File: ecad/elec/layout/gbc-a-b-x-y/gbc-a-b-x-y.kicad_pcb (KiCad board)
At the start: 2 copper layers, 10 parts

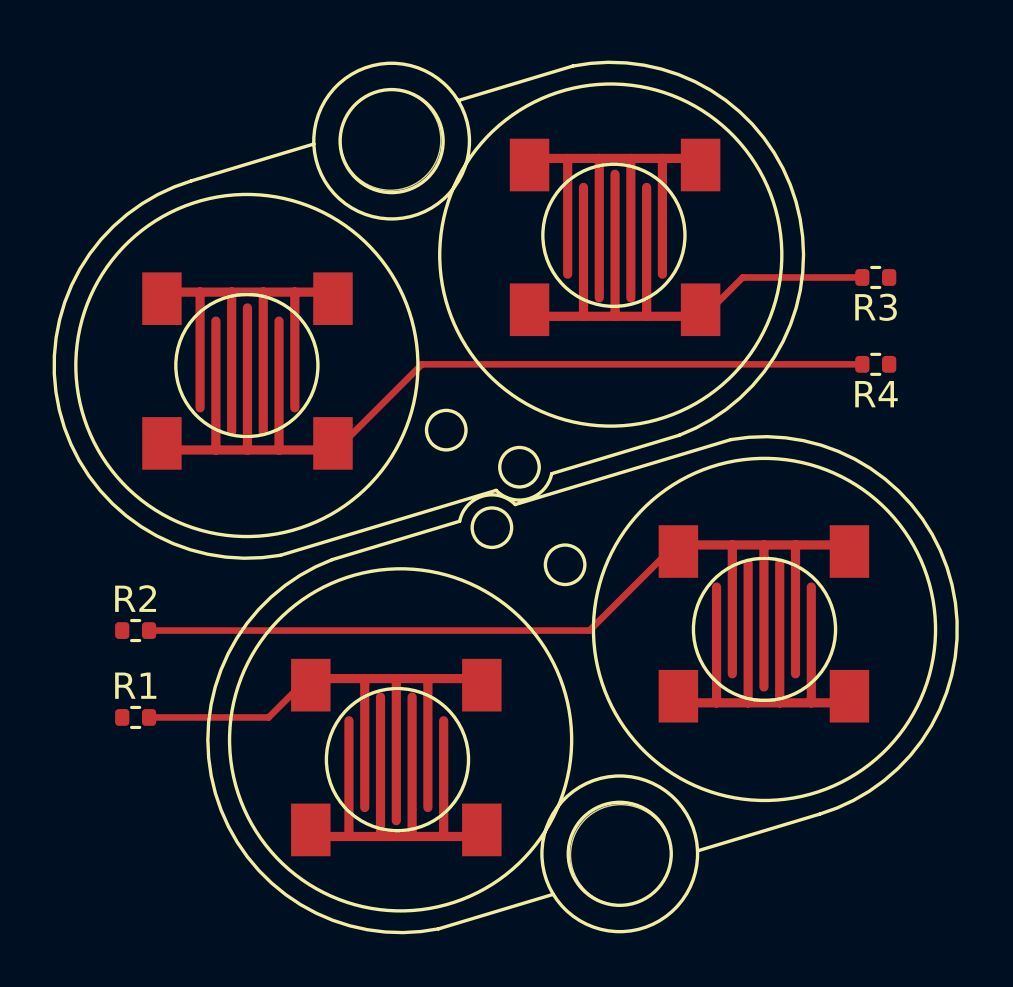
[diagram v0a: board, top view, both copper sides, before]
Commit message: update layouts to use latest footprints and fixed volume buttons and include address pins
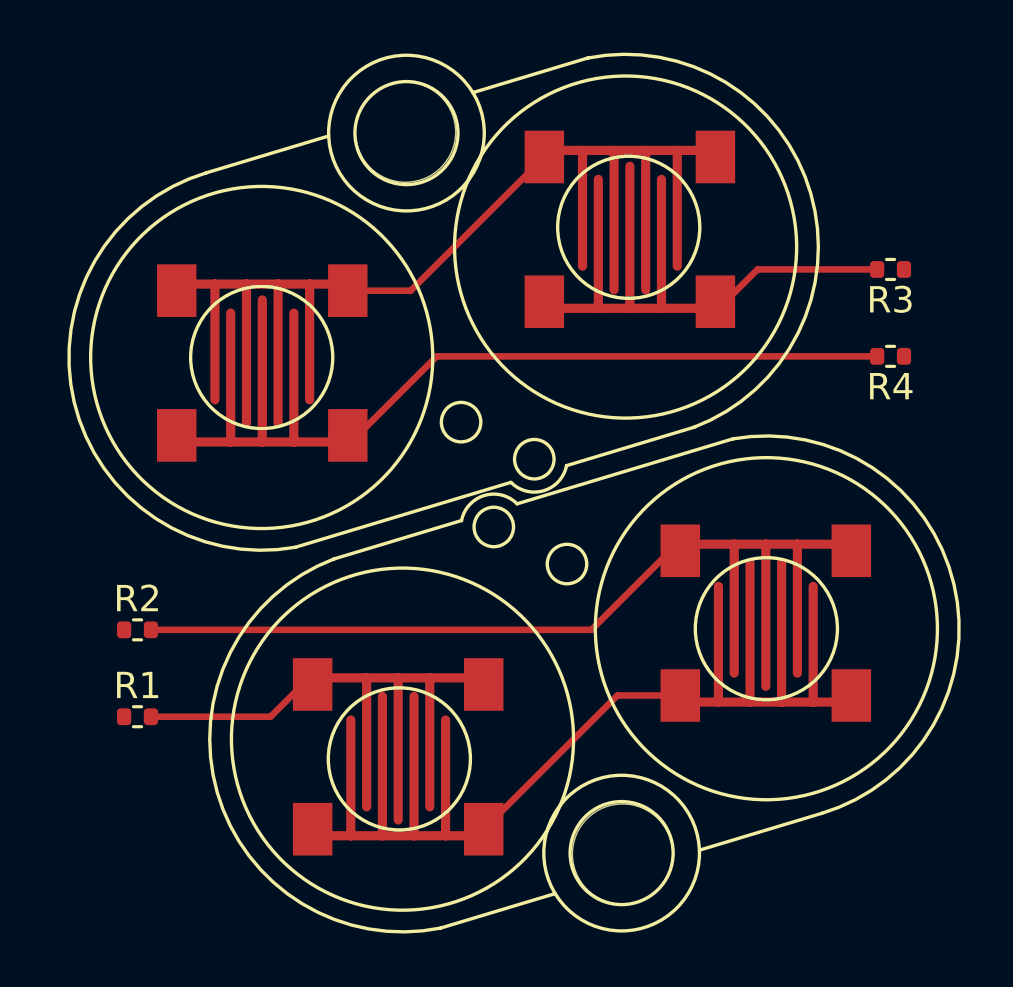
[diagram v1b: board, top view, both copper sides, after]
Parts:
- moved U4 0.64 mm to (179.2, 60.5)
- moved R3 0.64 mm to (196.1, 59.6)
- moved R4 0.64 mm to (196.1, 62.9)
- moved U5 0.64 mm to (186.2, 58.1)
- moved U6 0.64 mm to (172.3, 63.2)
- moved U2 0.08 mm to (177.4, 78.2)
- moved U3 0.08 mm to (191.4, 73.1)
- moved R1 0.08 mm to (167.5, 76.6)
- moved U1 0.08 mm to (184.4, 75.8)
- moved R2 0.08 mm to (167.5, 73.3)
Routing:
- net vcc: track 0.00 -> 19.1 mm

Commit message: Fix/atopile ecad (#82)
* fix(ecad): Fix bugs in atopile version of the design
* Add missing pullup resistors to AW9523 RSTN and INTN lines
* Fix I/O configuration for AW9523 so that all the inputs go to the same port pins as the previous version of the electronics

* minor cleanup to box3 after update to at 0.2.58

* fix udpate max17038 pullup to properly go to alert line after other fix

* typo

* update layout

* minor update to layout

* fix(buttons): pulldown -> pullup (so they are active low)

* update buttons to be pullup instead of pulldown; change led to be powered off VBUS instead of vbat

* update button footprints - start/select better aligned and all buttons have extra wires to ensure connections

* add net names and ensure packages are specified

* update box-emu-base layout

* update box-emu and box-3-emu layouts

* udpate to kicad 8

* add net name overrides and update all boards

* update atopile action to kicad 8

* comment out blender render
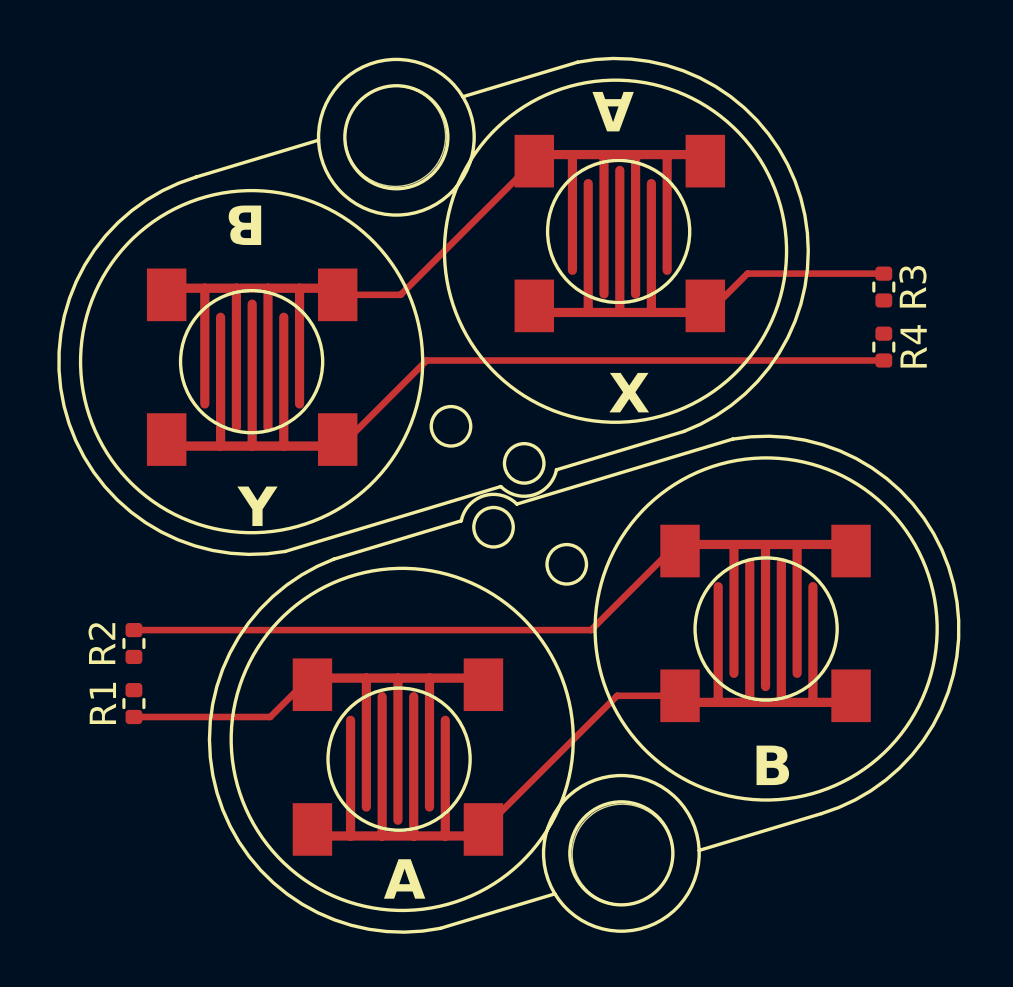
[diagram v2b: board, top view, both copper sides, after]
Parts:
- moved R3 0.72 mm to (195.9, 60.3), turned to 90 degrees
- moved R2 0.54 mm to (167.4, 73.9), turned to 90 degrees
- moved R1 0.52 mm to (167.4, 76.1), turned to -90 degrees
- moved R4 0.44 mm to (195.9, 62.6), turned to -90 degrees
- moved U4 0.41 mm to (178.9, 60.7)
- moved U6 0.41 mm to (171.9, 63.4)
- moved U5 0.41 mm to (185.9, 58.3)
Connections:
- R1 pad 1: gnd -> vcc
- R2 pad 1: gnd -> vcc
- R3 pad 1: gnd -> vcc
- R4 pad 1: gnd -> vcc
- U2 pad 2: vcc -> gnd
- U2 pad 4: vcc -> gnd
- U3 pad 2: vcc -> gnd
- U3 pad 4: vcc -> gnd
- U5 pad 2: vcc -> gnd
- U5 pad 4: vcc -> gnd
- U6 pad 2: vcc -> gnd
- U6 pad 4: vcc -> gnd
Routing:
- net gnd: track 0.00 -> 46.0 mm
- net vcc: track 19.1 -> 0.00 mm
- net x: track 6.28 -> 13.7 mm
- net a: track 6.28 -> 13.7 mm
- net y: track 21.0 -> 28.3 mm
- net b: track 21.0 -> 28.3 mm
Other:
- board text added: "A"
- board text added: "B"
- board text added: "X"
- board text added: "Y"
